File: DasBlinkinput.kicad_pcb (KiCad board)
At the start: 2 copper layers, 30 parts, among them P101 CONN_01X02, P102 CONN_01X01, P103 CONN_01X01, P104 CONN_01X05, U101 LP2980, U201 MCP6404, U202 LM339

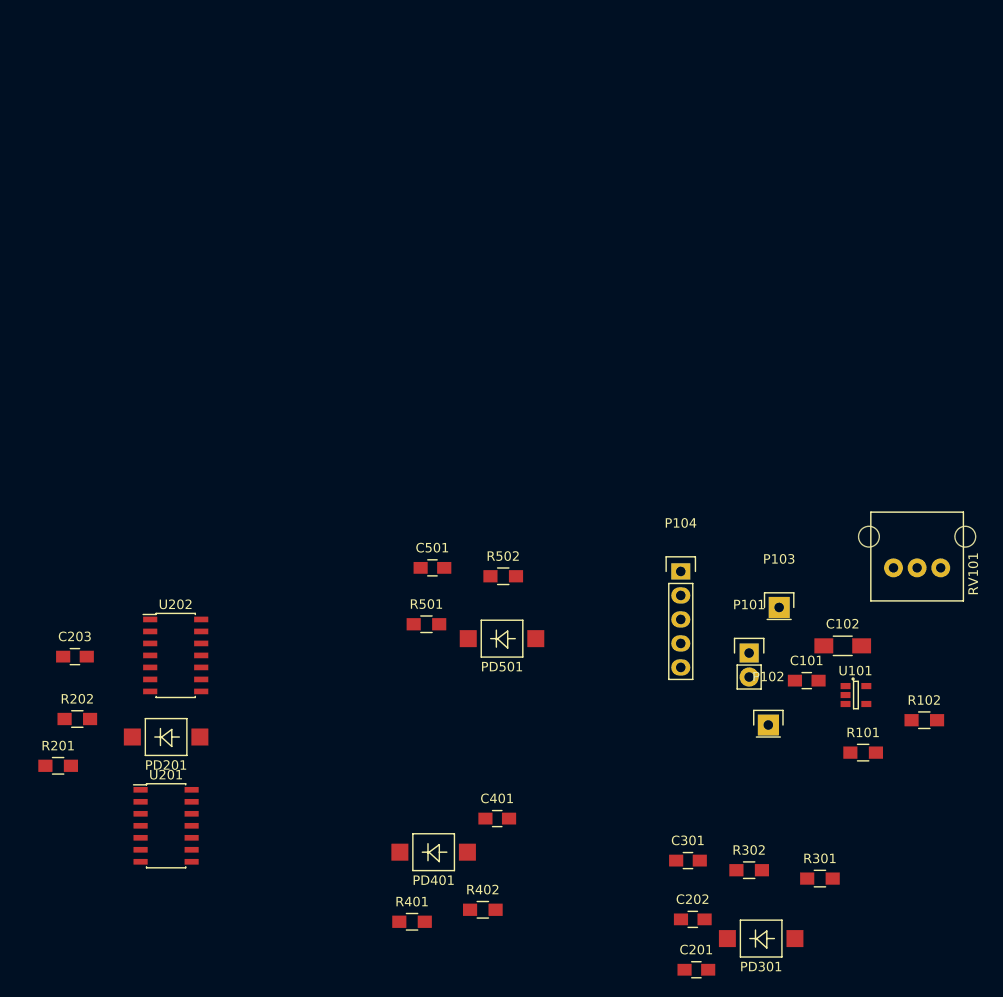
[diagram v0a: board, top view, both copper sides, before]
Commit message: added pull-up resistors
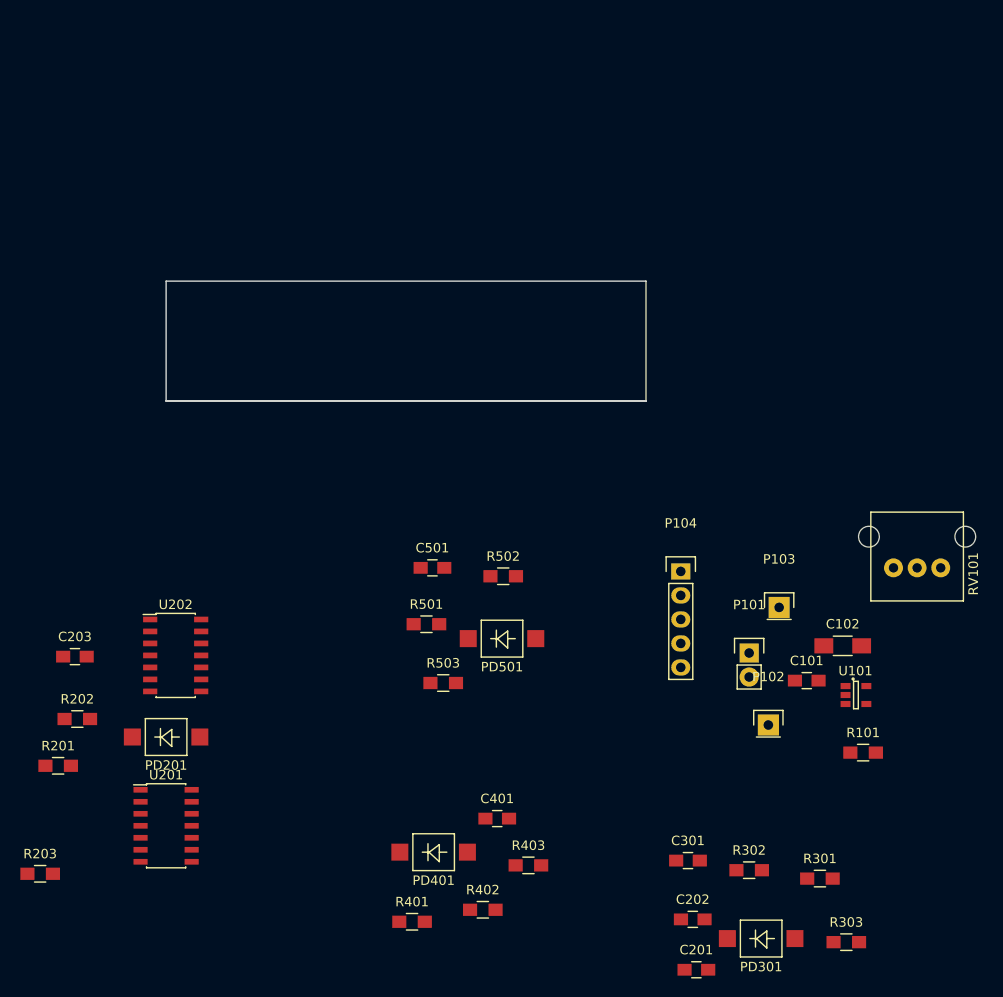
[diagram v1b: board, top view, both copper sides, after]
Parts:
- removed R102: 5K, Resistors_SMD:R_0805_HandSoldering
- added R203: 10K, Resistors_SMD:R_0805_HandSoldering, F.Cu at (95.9, 105.9)
- added R303: 10K, Resistors_SMD:R_0805_HandSoldering, F.Cu at (181.2, 113.2)
- added R403: 10K, Resistors_SMD:R_0805_HandSoldering, F.Cu at (147.6, 105.0)
- added R503: 10K, Resistors_SMD:R_0805_HandSoldering, F.Cu at (138.6, 85.7)
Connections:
- R101 pad 2: GND -> Net-(C101-Pad1)
- RV101 pad 3: Net-(R102-Pad1) -> +3V
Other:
- board outline added: 50.8 x 12.7 mm
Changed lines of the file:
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@@
 (kicad_pcb (version 4) (host pcbnew 4.0.2-stable)
   (general
-    (links 70)
-    (no_connects 70)
+    (links 77)
+    (no_connects 77)
     (area 0 0 0 0)
     (thickness 1.6)
-    (drawings 0)
+    (drawings 5)
     (tracks 0)
     (zones 0)
-    (modules 30)
-    (nets 20)
+    (modules 33)
+    (nets 19)
   )
   (page A4)
@@
   (net 15 /Channel4Photodetect/PD4)
   (net 16 "Net-(R101-Pad1)")
-  (net 17 "Net-(R102-Pad1)")
-  (net 18 /Channel1Photodetect/REF_V)
-  (net 19 "Net-(U101-Pad4)")
+  (net 17 /Channel1Photodetect/REF_V)
+  (net 18 "Net-(U101-Pad4)")
   (net_class Default "This is the default net class."
     (clearance 0.2)
@@
     (add_net "Net-(C501-Pad2)")
     (add_net "Net-(R101-Pad1)")
-    (add_net "Net-(R102-Pad1)")
     (add_net "Net-(U101-Pad4)")
   )
@@
       (net 16 "Net-(R101-Pad1)"))
     (pad 2 smd rect (at 1.35 0) (size 1.5 1.3) (layers F.Cu F.Paste F.Mask)
-      (net 2 GND))
-    (model Resistors_SMD.3dshapes/R_0805_HandSoldering.wrl
-      (at (xyz 0 0 0))
-      (scale (xyz 1 1 1))
-      (rotate (xyz 0 0 0))
-    )
-  )
-  (module Resistors_SMD:R_0805_HandSoldering (layer F.Cu)
-    (at 189.484 89.662)
-    (descr "Resistor SMD 0805, hand soldering")
-    (tags "resistor 0805")
-    (attr smd)
-    (fp_text reference R102 (at 0 -2.1) (layer F.SilkS)
-      (effects (font (size 1 1) (thickness 0.15)))
-    )
-    (fp_text value 5K (at 0 2.1) (layer F.Fab)
-      (effects (font (size 1 1) (thickness 0.15)))
-    )
-    (fp_line (start -2.4 -1) (end 2.4 -1) (layer F.CrtYd) (width 0.05))
-    (fp_line (start -2.4 1) (end 2.4 1) (layer F.CrtYd) (width 0.05))
-    (fp_line (start -2.4 -1) (end -2.4 1) (layer F.CrtYd) (width 0.05))
-    (fp_line (start 2.4 -1) (end 2.4 1) (layer F.CrtYd) (width 0.05))
-    (fp_line (start 0.6 0.875) (end -0.6 0.875) (layer F.SilkS) (width 0.15))
-    (fp_line (start -0.6 -0.875) (end 0.6 -0.875) (layer F.SilkS) (width 0.15))
-    (pad 1 smd rect (at -1.35 0) (size 1.5 1.3) (layers F.Cu F.Paste F.Mask)
-      (net 17 "Net-(R102-Pad1)"))
-    (pad 2 smd rect (at 1.35 0) (size 1.5 1.3) (layers F.Cu F.Paste F.Mask)
-      (net 3 +3V))
+      (net 1 "Net-(C101-Pad1)"))
     (model Resistors_SMD.3dshapes/R_0805_HandSoldering.wrl
       (at (xyz 0 0 0))
@@
     (fp_line (start -4.9 -5.9) (end -4.9 3.5) (layer F.SilkS) (width 0.15))
     (pad 3 thru_hole circle (at 2.5 0) (size 2 2) (drill 1) (layers *.Cu *.Mask F.SilkS)
-      (net 17 "Net-(R102-Pad1)"))
+      (net 3 +3V))
     (pad 2 thru_hole circle (at 0 0) (size 2 2) (drill 1) (layers *.Cu *.Mask F.SilkS)
-      (net 18 /Channel1Photodetect/REF_V))
+      (net 17 /Channel1Photodetect/REF_V))
     (pad 1 thru_hole circle (at -2.5 0) (size 2 2) (drill 1) (layers *.Cu *.Mask F.SilkS)
       (net 2 GND))
@@
       (net 16 "Net-(R101-Pad1)"))
     (pad 4 smd rect (at 1.1 0.95) (size 1.06 0.65) (layers F.Cu F.Paste F.Mask)
-      (net 19 "Net-(U101-Pad4)"))
+      (net 18 "Net-(U101-Pad4)"))
     (pad 5 smd rect (at 1.1 -0.95) (size 1.06 0.65) (layers F.Cu F.Paste F.Mask)
       (net 3 +3V))
@@
       (net 3 +3V))
     (pad 4 smd rect (at -2.7 0) (size 1.5 0.6) (layers F.Cu F.Paste F.Mask)
-      (net 18 /Channel1Photodetect/REF_V))
+      (net 17 /Channel1Photodetect/REF_V))
     (pad 5 smd rect (at -2.7 1.27) (size 1.5 0.6) (layers F.Cu F.Paste F.Mask)
       (net 4 "Net-(C202-Pad1)"))
     (pad 6 smd rect (at -2.7 2.54) (size 1.5 0.6) (layers F.Cu F.Paste F.Mask)
-      (net 18 /Channel1Photodetect/REF_V))
+      (net 17 /Channel1Photodetect/REF_V))
     (pad 7 smd rect (at -2.7 3.81) (size 1.5 0.6) (layers F.Cu F.Paste F.Mask)
       (net 6 "Net-(C301-Pad1)"))
     (pad 8 smd rect (at 2.7 3.81) (size 1.5 0.6) (layers F.Cu F.Paste F.Mask)
-      (net 18 /Channel1Photodetect/REF_V))
+      (net 17 /Channel1Photodetect/REF_V))
     (pad 9 smd rect (at 2.7 2.54) (size 1.5 0.6) (layers F.Cu F.Paste F.Mask)
       (net 10 "Net-(C501-Pad1)"))
     (pad 10 smd rect (at 2.7 1.27) (size 1.5 0.6) (layers F.Cu F.Paste F.Mask)
-      (net 18 /Channel1Photodetect/REF_V))
+      (net 17 /Channel1Photodetect/REF_V))
     (pad 11 smd rect (at 2.7 0) (size 1.5 0.6) (layers F.Cu F.Paste F.Mask)
       (net 8 "Net-(C401-Pad1)"))
@@
     )
   )
+  (module Resistors_SMD:R_0805_HandSoldering (layer F.Cu)
+    (at 95.885 105.918)
+    (descr "Resistor SMD 0805, hand soldering")
+    (tags "resistor 0805")
+    (attr smd)
+    (fp_text reference R203 (at 0 -2.1) (layer F.SilkS)
+      (effects (font (size 1 1) (thickness 0.15)))
+    )
+    (fp_text value 10K (at 0 2.1) (layer F.Fab)
+      (effects (font (size 1 1) (thickness 0.15)))
+    )
+    (fp_line (start -2.4 -1) (end 2.4 -1) (layer F.CrtYd) (width 0.05))
+    (fp_line (start -2.4 1) (end 2.4 1) (layer F.CrtYd) (width 0.05))
+    (fp_line (start -2.4 -1) (end -2.4 1) (layer F.CrtYd) (width 0.05))
+    (fp_line (start 2.4 -1) (end 2.4 1) (layer F.CrtYd) (width 0.05))
+    (fp_line (start 0.6 0.875) (end -0.6 0.875) (layer F.SilkS) (width 0.15))
+    (fp_line (start -0.6 -0.875) (end 0.6 -0.875) (layer F.SilkS) (width 0.15))
+    (pad 1 smd rect (at -1.35 0) (size 1.5 1.3) (layers F.Cu F.Paste F.Mask)
+      (net 12 /Channel1Photodetect/PD1))
+    (pad 2 smd rect (at 1.35 0) (size 1.5 1.3) (layers F.Cu F.Paste F.Mask)
+      (net 3 +3V))
+    (model Resistors_SMD.3dshapes/R_0805_HandSoldering.wrl
+      (at (xyz 0 0 0))
+      (scale (xyz 1 1 1))
+      (rotate (xyz 0 0 0))
+    )
+  )
+  (module Resistors_SMD:R_0805_HandSoldering (layer F.Cu)
+    (at 181.229 113.157)
+    (descr "Resistor SMD 0805, hand soldering")
+    (tags "resistor 0805")
+    (attr smd)
+    (fp_text reference R303 (at 0 -2.1) (layer F.SilkS)
+      (effects (font (size 1 1) (thickness 0.15)))
+    )
+    (fp_text value 10K (at 0 2.1) (layer F.Fab)
+      (effects (font (size 1 1) (thickness 0.15)))
+    )
+    (fp_line (start -2.4 -1) (end 2.4 -1) (layer F.CrtYd) (width 0.05))
+    (fp_line (start -2.4 1) (end 2.4 1) (layer F.CrtYd) (width 0.05))
+    (fp_line (start -2.4 -1) (end -2.4 1) (layer F.CrtYd) (width 0.05))
+    (fp_line (start 2.4 -1) (end 2.4 1) (layer F.CrtYd) (width 0.05))
+    (fp_line (start 0.6 0.875) (end -0.6 0.875) (layer F.SilkS) (width 0.15))
+    (fp_line (start -0.6 -0.875) (end 0.6 -0.875) (layer F.SilkS) (width 0.15))
+    (pad 1 smd rect (at -1.35 0) (size 1.5 1.3) (layers F.Cu F.Paste F.Mask)
+      (net 13 /Channel2Photodetect/PD2))
+    (pad 2 smd rect (at 1.35 0) (size 1.5 1.3) (layers F.Cu F.Paste F.Mask)
+      (net 3 +3V))
+    (model Resistors_SMD.3dshapes/R_0805_HandSoldering.wrl
+      (at (xyz 0 0 0))
+      (scale (xyz 1 1 1))
+      (rotate (xyz 0 0 0))
+    )
+  )
+  (module Resistors_SMD:R_0805_HandSoldering (layer F.Cu)
+    (at 147.574 105.029)
+    (descr "Resistor SMD 0805, hand soldering")
+    (tags "resistor 0805")
+    (attr smd)
+    (fp_text reference R403 (at 0 -2.1) (layer F.SilkS)
+      (effects (font (size 1 1) (thickness 0.15)))
+    )
+    (fp_text value 10K (at 0 2.1) (layer F.Fab)
+      (effects (font (size 1 1) (thickness 0.15)))
+    )
+    (fp_line (start -2.4 -1) (end 2.4 -1) (layer F.CrtYd) (width 0.05))
+    (fp_line (start -2.4 1) (end 2.4 1) (layer F.CrtYd) (width 0.05))
+    (fp_line (start -2.4 -1) (end -2.4 1) (layer F.CrtYd) (width 0.05))
+    (fp_line (start 2.4 -1) (end 2.4 1) (layer F.CrtYd) (width 0.05))
+    (fp_line (start 0.6 0.875) (end -0.6 0.875) (layer F.SilkS) (width 0.15))
+    (fp_line (start -0.6 -0.875) (end 0.6 -0.875) (layer F.SilkS) (width 0.15))
+    (pad 1 smd rect (at -1.35 0) (size 1.5 1.3) (layers F.Cu F.Paste F.Mask)
+      (net 14 /Channel3Photodetect/PD3))
+    (pad 2 smd rect (at 1.35 0) (size 1.5 1.3) (layers F.Cu F.Paste F.Mask)
+      (net 3 +3V))
+    (model Resistors_SMD.3dshapes/R_0805_HandSoldering.wrl
+      (at (xyz 0 0 0))
+      (scale (xyz 1 1 1))
+      (rotate (xyz 0 0 0))
+    )
+  )
+  (module Resistors_SMD:R_0805_HandSoldering (layer F.Cu)
+    (at 138.557 85.725)
+    (descr "Resistor SMD 0805, hand soldering")
+    (tags "resistor 0805")
+    (attr smd)
+    (fp_text reference R503 (at 0 -2.1) (layer F.SilkS)
+      (effects (font (size 1 1) (thickness 0.15)))
+    )
+    (fp_text value 10K (at 0 2.1) (layer F.Fab)
+      (effects (font (size 1 1) (thickness 0.15)))
+    )
+    (fp_line (start -2.4 -1) (end 2.4 -1) (layer F.CrtYd) (width 0.05))
+    (fp_line (start -2.4 1) (end 2.4 1) (layer F.CrtYd) (width 0.05))
+    (fp_line (start -2.4 -1) (end -2.4 1) (layer F.CrtYd) (width 0.05))
+    (fp_line (start 2.4 -1) (end 2.4 1) (layer F.CrtYd) (width 0.05))
+    (fp_line (start 0.6 0.875) (end -0.6 0.875) (layer F.SilkS) (width 0.15))
+    (fp_line (start -0.6 -0.875) (end 0.6 -0.875) (layer F.SilkS) (width 0.15))
+    (pad 1 smd rect (at -1.35 0) (size 1.5 1.3) (layers F.Cu F.Paste F.Mask)
+      (net 15 /Channel4Photodetect/PD4))
+    (pad 2 smd rect (at 1.35 0) (size 1.5 1.3) (layers F.Cu F.Paste F.Mask)
+      (net 3 +3V))
+    (model Resistors_SMD.3dshapes/R_0805_HandSoldering.wrl
+      (at (xyz 0 0 0))
+      (scale (xyz 1 1 1))
+      (rotate (xyz 0 0 0))
+    )
+  )
+  (gr_line (start 160.02 55.88) (end 160.02 43.18) (angle 90) (layer Edge.Cuts) (width 0.15))
+  (gr_line (start 109.22 55.88) (end 160.02 55.88) (angle 90) (layer Edge.Cuts) (width 0.15))
+  (gr_line (start 109.22 43.18) (end 109.22 55.88) (angle 90) (layer Edge.Cuts) (width 0.15))
+  (gr_line (start 109.22 43.18) (end 160.02 43.18) (angle 90) (layer Edge.Cuts) (width 0.15))
+  (gr_line (start 109.22 55.88) (end 160.02 55.88) (angle 90) (layer Edge.Cuts) (width 0.15))
 )

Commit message: expanded and rotated board
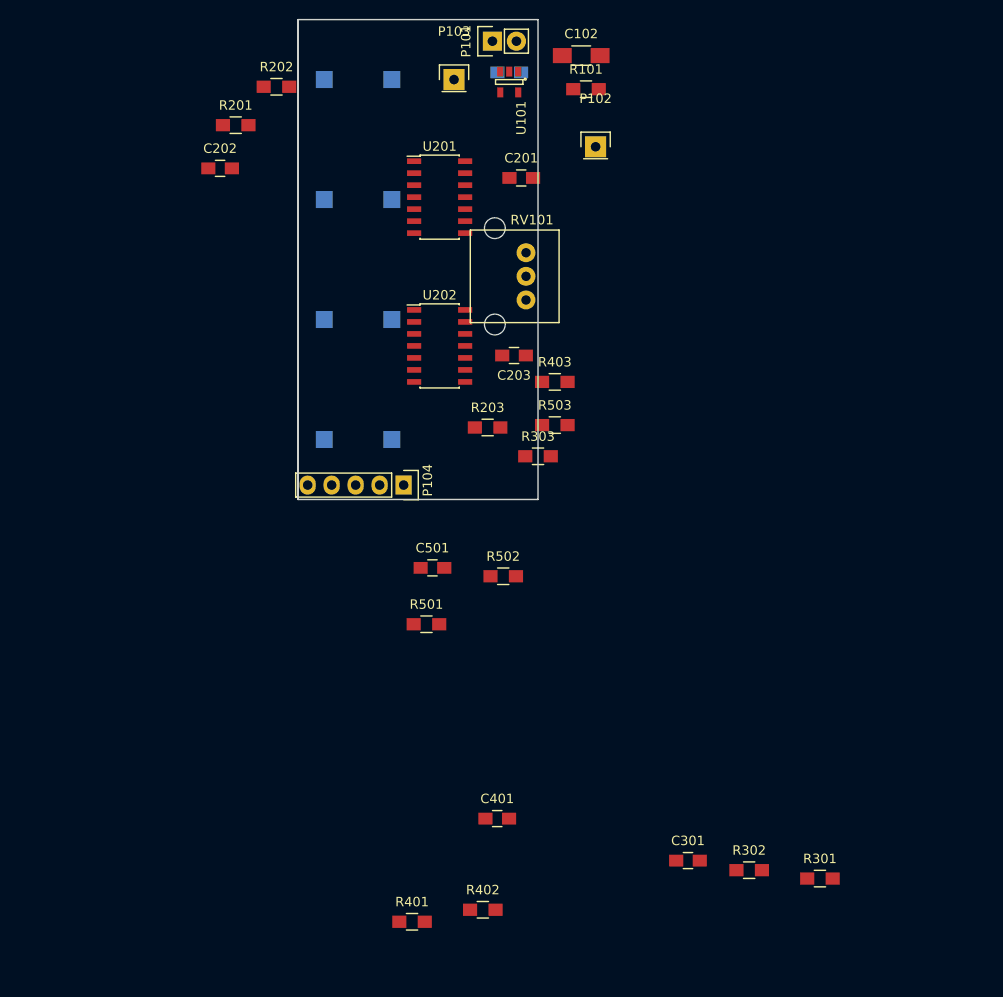
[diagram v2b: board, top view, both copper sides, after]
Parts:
- C101, PD201, PD301, PD401, PD501: moved to B.Cu
- moved C202 93.9 mm to (114.9, 31.2)
- moved PD301 89.1 mm to (129.5, 34.5), turned to 180 degrees
- moved C201 85.8 mm to (146.8, 32.3)
- moved R101 76.1 mm to (153.7, 22.9)
- moved U101 74.6 mm to (145.5, 22.1), turned to 270 degrees
- moved U201 72.6 mm to (138.2, 34.3)
- moved PD201 72.5 mm to (129.5, 21.8), turned to 180 degrees
- moved C101 71.7 mm to (145.5, 21.1), turned to 180 degrees
- moved R201 70.4 mm to (116.6, 26.7)
- moved P101 70.2 mm to (143.8, 17.8), turned to 90 degrees
- moved R202 70.2 mm to (120.9, 22.6)
- moved C102 68.3 mm to (153.2, 19.3)
- moved R203 66.9 mm to (143.3, 58.7)
- moved P103 65.6 mm to (139.7, 21.8)
- moved P102 63.9 mm to (154.7, 29.0)
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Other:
- board size 50.8 x 12.7 mm -> 25.4 x 50.8 mm
- copper layers 2 -> 4
- net class Default: clearance 0.2 -> 0.1524; trace_width 0.25 -> 0.1524; via_dia 0.6 -> 0.6858; via_drill 0.4 -> 0.3302
- net class Power added: clearance 0.254, trace_width 0.6096, via_dia 0.889, via_drill 0.3302
- rule trace_clearance: 0.2 -> 0.1524
- rule trace_min: 0.2 -> 0.1524
- rule via_min_drill: 0.3 -> 0.3302
- rule via_min_size: 0.4 -> 0.6858
